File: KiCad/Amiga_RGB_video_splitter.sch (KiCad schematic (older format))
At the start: 11 parts, among them J1 DB23_Female-Connector, J2 DB15_Female_HighDensity_Mount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, J3 KMDGX-9S-BS-1, J4 PJ-320A, U1 THS7374IPWR, U2 74HCT2G17

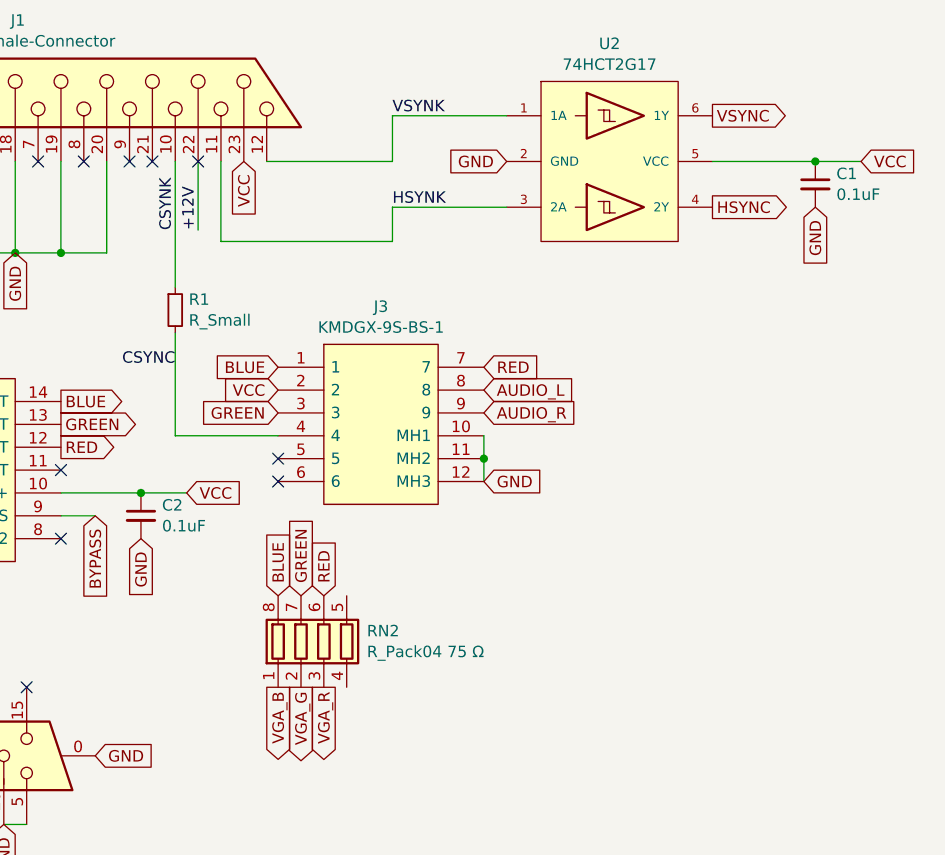
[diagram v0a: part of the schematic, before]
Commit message: Change C1 to C2 and C2 to C3 and adding resistor Ohm values on silkscreen
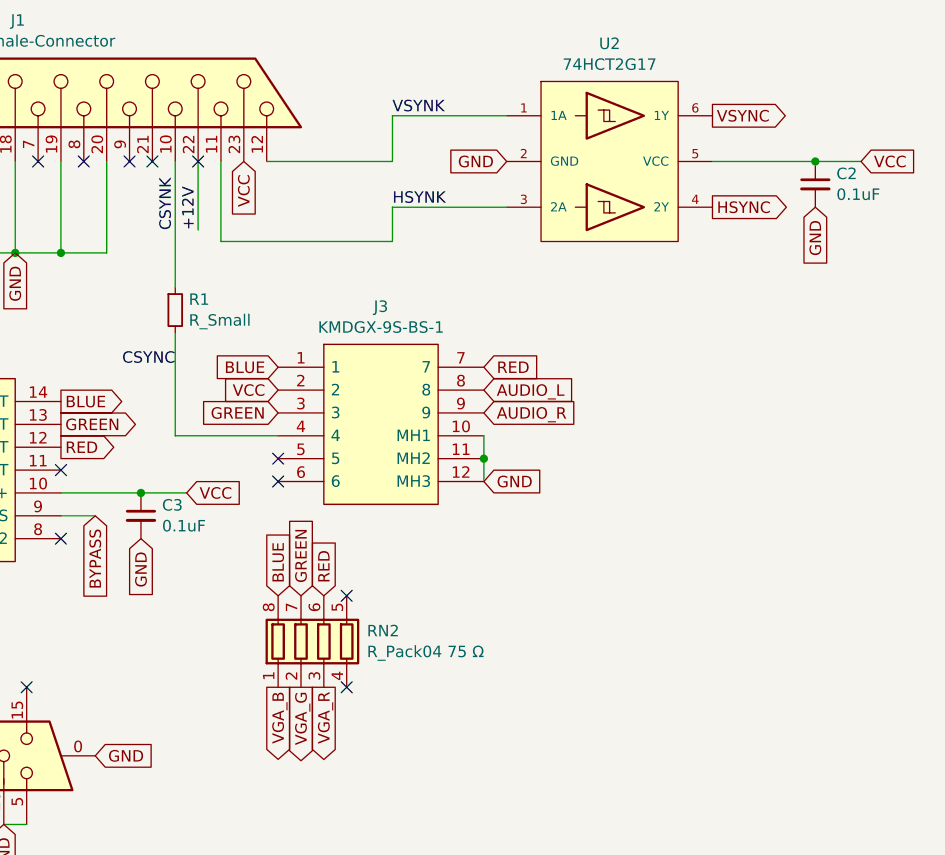
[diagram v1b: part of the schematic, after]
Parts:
- renumbered C1 to C2, C2 to C3
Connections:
- no-connect marks 22 -> 24
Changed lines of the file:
@@
 VCC
 $Comp
-L Device:C_Small C2
+L Device:C_Small C3
 U 1 1 6832D346
 P 4150 4250
-F 0 "C2" H 4242 4296 50  0000 L CNN
+F 0 "C3" H 4242 4296 50  0000 L CNN
 F 1 "0.1uF" H 4242 4205 50  0000 L CNN
 F 2 "Capacitor_SMD:C_0805_2012Metric_Pad1.18x1.45mm_HandSolder" H 4150 4250 50  0001 C CNN
@@
 VCC
 $Comp
-L Device:C_Small C1
+L Device:C_Small C2
 U 1 1 68348604
 P 7100 2800
-F 0 "C1" H 7192 2846 50  0000 L CNN
+F 0 "C2" H 7192 2846 50  0000 L CNN
 F 1 "0.1uF" H 7192 2755 50  0000 L CNN
 F 2 "Capacitor_SMD:C_0805_2012Metric_Pad1.18x1.45mm_HandSolder" H 7100 2800 50  0001 C CNN
@@
 Text Label 5250 2900 0    50   ~ 0
 HSYNK
+NoConn ~ 5050 4600
+NoConn ~ 5050 5000
 $EndSCHEMATC

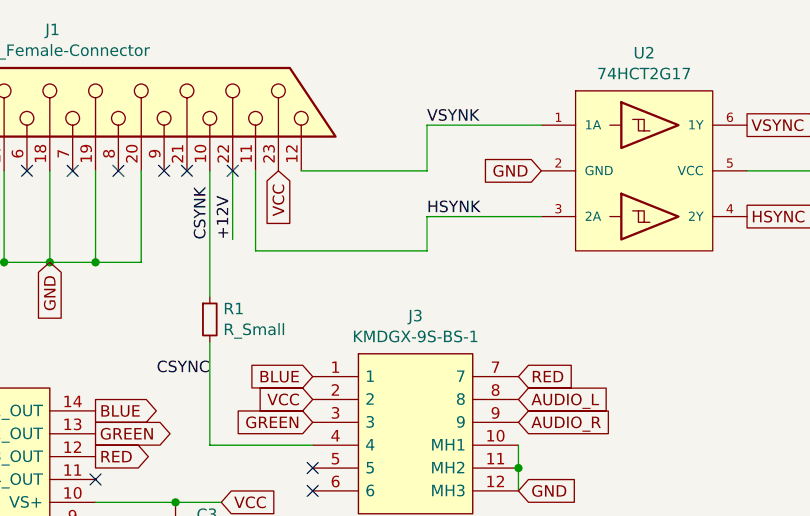
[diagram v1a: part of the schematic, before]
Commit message: Add polarized TH-capacitor C1 100uF Radial pitch 2.5 mm
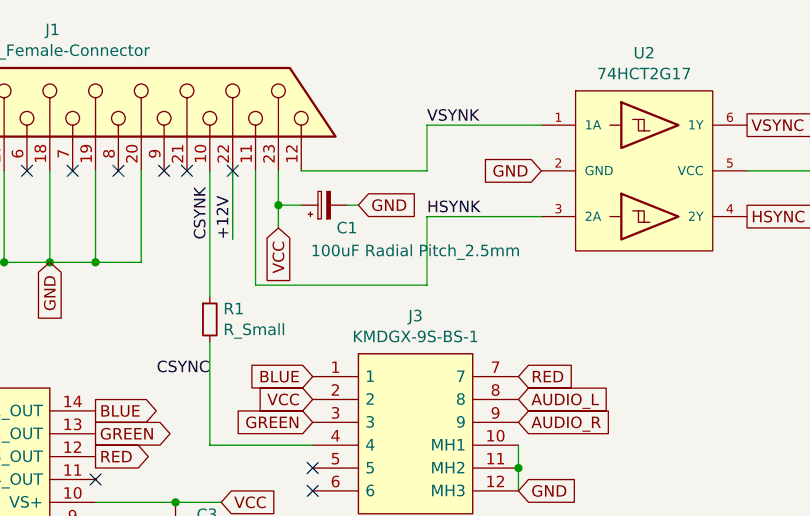
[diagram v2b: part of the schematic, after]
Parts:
- added C1: 100uF Radial Pitch_2.5mm, Capacitor_THT:CP_Radial_D5.0mm_P2.50mm, symbol Device:CP_Small
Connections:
- net +5V: now also C1.1
- net GND: now also C1.2
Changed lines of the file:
@@
 	5650 4000 5650 4100
 Connection ~ 5650 4000
-Text GLabel 4600 2700 3    50   Input ~ 0
+Text GLabel 4600 2950 3    50   Input ~ 0
 VCC
 Text GLabel 2900 2700 3    50   Input ~ 0
@@
 	6650 2700 7100 2700
 Wire Wire Line
-	4500 2700 4500 3050
-Wire Wire Line
-	4500 3050 5250 3050
-Wire Wire Line
-	5250 3050 5250 2900
-Wire Wire Line
 	5250 2900 5750 2900
 Text Label 5250 2900 0    50   ~ 0
@@
 NoConn ~ 5050 4600
 NoConn ~ 5050 5000
+$Comp
+L Device:CP_Small C1
+U 1 1 6834FAFC
+P 4800 2850
+F 0 "C1" V 4700 2750 50  0000 C CNN
+F 1 "100uF Radial Pitch_2.5mm" V 4600 2450 50  0000 C CNN
+F 2 "Capacitor_THT:CP_Radial_D5.0mm_P2.50mm" H 4800 2850 50  0001 C CNN
+F 3 "~" H 4800 2850 50  0001 C CNN
+	1    4800 2850
+	0    -1   -1   0
+$EndComp
+Text GLabel 4950 2850 2    50   Input ~ 0
+GND
+Wire Wire Line
+	4950 2850 4900 2850
+Wire Wire Line
+	4500 3200 5250 3200
+Wire Wire Line
+	5250 2900 5250 3200
+Wire Wire Line
+	4500 2700 4500 3200
+Wire Wire Line
+	4600 2700 4600 2850
+Wire Wire Line
+	4700 2850 4600 2850
+Connection ~ 4600 2850
+Wire Wire Line
+	4600 2850 4600 2950
 $EndSCHEMATC

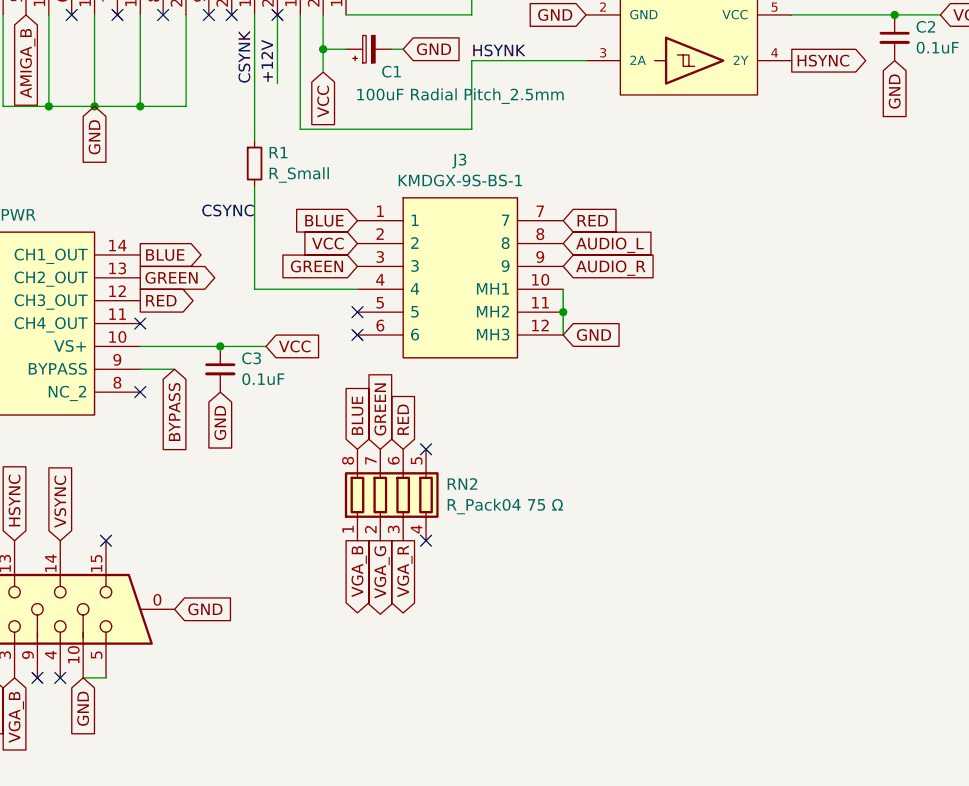
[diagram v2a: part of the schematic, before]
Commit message: Add 10k pull-up resistor R2 for BYPASS signal going to MSS22D18 3-Pin slide toggle switch
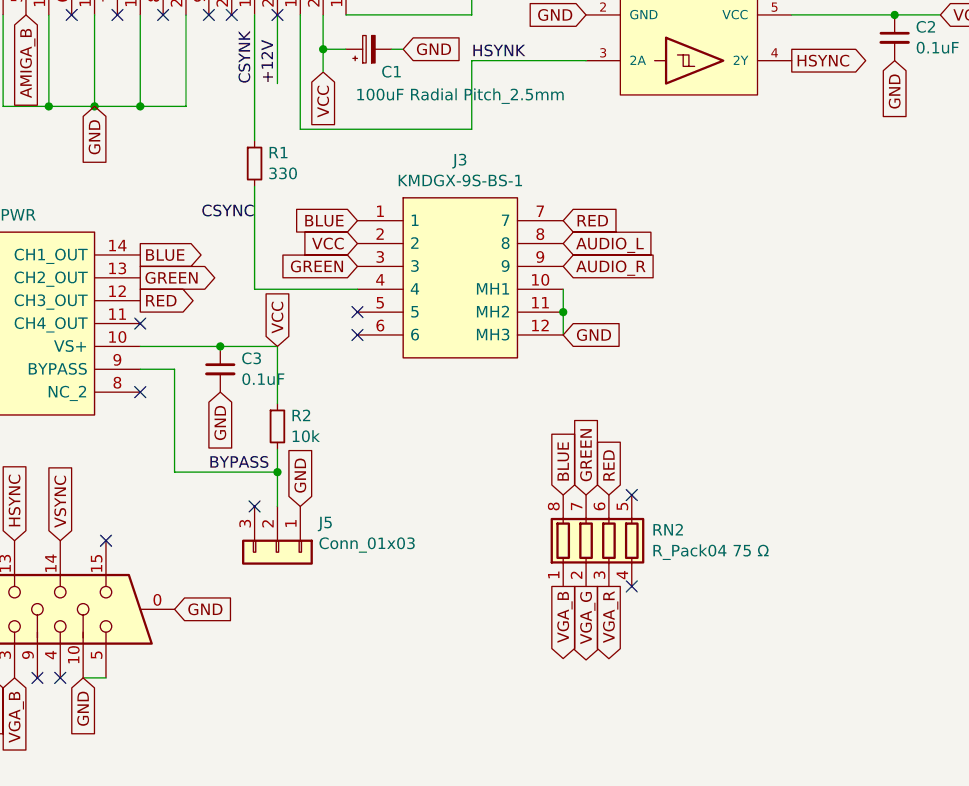
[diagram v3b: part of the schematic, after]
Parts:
- added J5: Conn_01x03, Amiga_RGB_video_splitter:PinHeader_1x03_P2.5mm_Vertical, symbol Connector_Generic:Conn_01x03
- added R2: 10k, Resistor_SMD:R_1206_3216Metric_Pad1.30x1.75mm_HandSolder, symbol Device:R_Small
- R1: value R_Small -> 330
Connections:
- net +5V: now also R2.1
- net BYPASS: now also J5.2 (Pin_2), R2.2
- net GND: now also J5.1 (Pin_1)
- no-connect marks 24 -> 25
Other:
- moved on the sheet: RN2
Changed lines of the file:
@@
 NoConn ~ 2400 4350
 NoConn ~ 3800 4350
-Text GLabel 4350 4150 2    50   Input ~ 0
+Text GLabel 4400 4150 1    50   Input ~ 0
 VCC
 $Comp
@@
 GND
 Connection ~ 4150 4150
-Wire Wire Line
-	4150 4150 4350 4150
 NoConn ~ 3450 5600
 NoConn ~ 2850 5000
@@
 P 4300 3350
 F 0 "R1" H 4359 3396 50  0000 L CNN
-F 1 "R_Small" H 4359 3305 50  0000 L CNN
+F 1 "330" H 4359 3305 50  0000 L CNN
 F 2 "Resistor_SMD:R_1206_3216Metric_Pad1.30x1.75mm_HandSolder" H 4300 3350 50  0001 C CNN
 F 3 "~" H 4300 3350 50  0001 C CNN
@@
 	2400 4250 2400 4150
 Connection ~ 2400 4150
-Text GLabel 3950 4250 3    50   Input ~ 0
-BYPASS
 Wire Wire Line
 	3800 4150 4150 4150
@@
 L Device:R_Pack04 RN2
 U 1 1 68354B66
-P 4950 4800
-F 0 "RN2" H 5138 4846 50  0000 L CNN
-F 1 "R_Pack04 75 Ω" H 5138 4755 50  0000 L CNN
-F 2 "Amiga_RGB_video_splitter:RESCAF80P320X160X60-8N" V 5225 4800 50  0001 C CNN
-F 3 "~" H 4950 4800 50  0001 C CNN
-	1    4950 4800
-	1    0    0    -1
-$EndComp
-Text GLabel 4750 4600 1    50   Input ~ 0
+P 5850 5000
+F 0 "RN2" H 6038 5046 50  0000 L CNN
+F 1 "R_Pack04 75 Ω" H 6038 4955 50  0000 L CNN
+F 2 "Amiga_RGB_video_splitter:RESCAF80P320X160X60-8N" V 6125 5000 50  0001 C CNN
+F 3 "~" H 5850 5000 50  0001 C CNN
+	1    5850 5000
+	1    0    0    -1
+$EndComp
+Text GLabel 5650 4800 1    50   Input ~ 0
 BLUE
-Text GLabel 4850 4600 1    50   Input ~ 0
+Text GLabel 5750 4800 1    50   Input ~ 0
 GREEN
-Text GLabel 4950 4600 1    50   Input ~ 0
+Text GLabel 5850 4800 1    50   Input ~ 0
 RED
-Text GLabel 4750 5000 3    50   Output ~ 0
+Text GLabel 5650 5200 3    50   Output ~ 0
 VGA_B
-Text GLabel 4850 5000 3    50   Output ~ 0
+Text GLabel 5750 5200 3    50   Output ~ 0
 VGA_G
-Text GLabel 4950 5000 3    50   Output ~ 0
+Text GLabel 5850 5200 3    50   Output ~ 0
 VGA_R
 $Comp
@@
 Text Label 5250 2900 0    50   ~ 0
 HSYNK
-NoConn ~ 5050 4600
-NoConn ~ 5050 5000
+NoConn ~ 5950 4800
+NoConn ~ 5950 5200
 $Comp
 L Device:CP_Small C1
@@
 Wire Wire Line
 	4600 2850 4600 2950
+$Comp
+L Connector_Generic:Conn_01x03 J5
+U 1 1 6835D390
+P 4400 5050
+F 0 "J5" V 4272 5230 50  0000 L CNN
+F 1 "Conn_01x03" V 4363 5230 50  0000 L CNN
+F 2 "Amiga_RGB_video_splitter:PinHeader_1x03_P2.5mm_Vertical" H 4400 5050 50  0001 C CNN
+F 3 "~" H 4400 5050 50  0001 C CNN
+	1    4400 5050
+	0    1    1    0
+$EndComp
+Wire Wire Line
+	3950 4250 3950 4700
+Wire Wire Line
+	3950 4700 4400 4700
+Wire Wire Line
+	4400 4700 4400 4850
+Text Label 4100 4700 0    50   ~ 0
+BYPASS
+Text GLabel 4500 4850 1    50   Input ~ 0
+GND
+NoConn ~ 4300 4850
+$Comp
+L Device:R_Small R2
+U 1 1 6836E687
+P 4400 4500
+F 0 "R2" H 4459 4546 50  0000 L CNN
+F 1 "10k" H 4459 4455 50  0000 L CNN
+F 2 "Resistor_SMD:R_1206_3216Metric_Pad1.30x1.75mm_HandSolder" H 4400 4500 50  0001 C CNN
+F 3 "~" H 4400 4500 50  0001 C CNN
+	1    4400 4500
+	1    0    0    -1
+$EndComp
+Wire Wire Line
+	4150 4150 4400 4150
+Wire Wire Line
+	4400 4150 4400 4400
+Wire Wire Line
+	4400 4600 4400 4700
+Connection ~ 4400 4700
 $EndSCHEMATC
